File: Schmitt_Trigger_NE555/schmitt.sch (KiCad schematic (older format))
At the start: 8 parts, among them J1 CONN_01X02, J2 Vcc, U1 LM555N

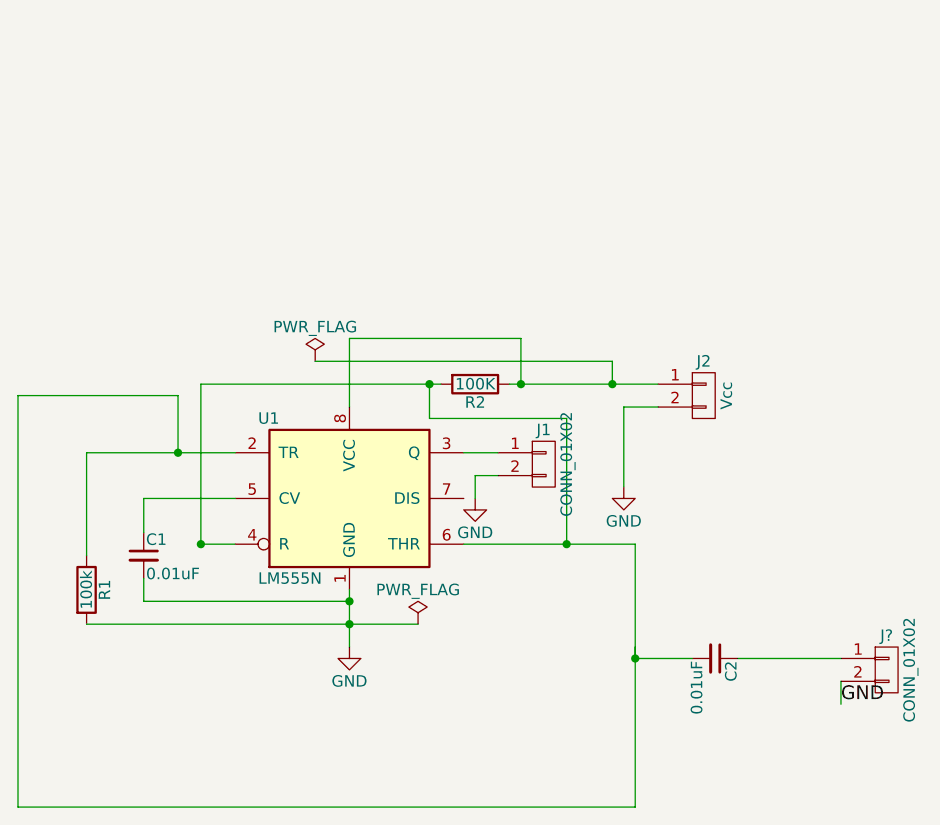
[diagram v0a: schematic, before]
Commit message: Added Schmitt Trigger Using NE555 PCB Layout
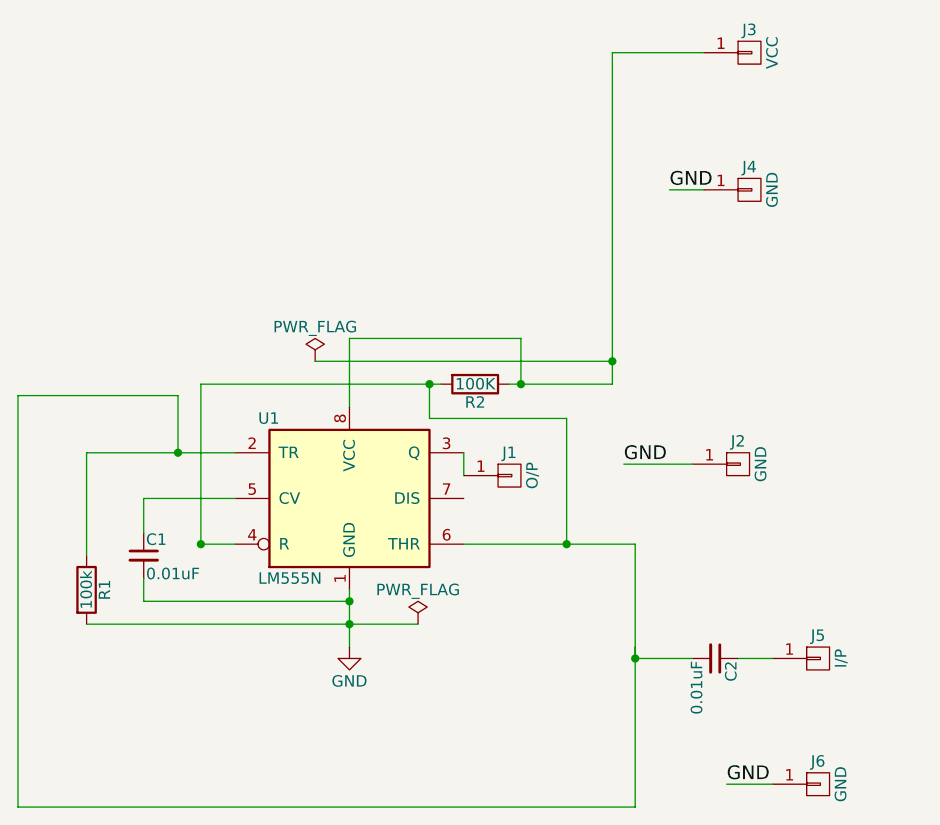
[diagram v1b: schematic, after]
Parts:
- removed J1: CONN_01X02, Connectors_Terminal_Blocks:TerminalBlock_Pheonix_MKDS1.5-2pol, symbol CONN_01X02
- removed J2: Vcc, Connectors_Terminal_Blocks:TerminalBlock_Pheonix_MKDS1.5-2pol, symbol CONN_01X02
- removed J?: CONN_01X02, symbol CONN_01X02
- added J1: O/P, Connectors:Banana_Jack_1Pin, symbol CONN_01X01
- added J2, J4, J6: GND, Connectors:Banana_Jack_1Pin, symbol CONN_01X01
- added J3: VCC, Connectors:Banana_Jack_1Pin, symbol CONN_01X01
- added J5: I/P, Connectors:Banana_Jack_1Pin, symbol CONN_01X01
- R1, R2: footprint (none) -> Resistors_THT:R_Axial_DIN0207_L6.3mm_D2.5mm_P15.24mm_Horizontal
- U1: footprint (none) -> Housings_DIP:DIP-8_W7.62mm
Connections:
- net GND: now also J2.1 (P1), J4.1 (P1), J6.1 (P1)
- net at U1.3 (Q): now also J1.1 (P1)
- net at R2.1, U1.8 (VCC): now also J3.1 (P1)
- net at C2.1: now also J5.1 (P1)
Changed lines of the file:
@@
 LIBS:contrib
 LIBS:valves
+LIBS:schmitt-cache
 EELAYER 25 0
 EELAYER END
@@
 F 0 "U1" H 6100 4800 50  0000 L CNN
 F 1 "LM555N" H 6100 4100 50  0000 L CNN
-F 2 "" H 6500 4450 50  0001 C CNN
+F 2 "Housings_DIP:DIP-8_W7.62mm" H 6500 4450 50  0001 C CNN
 F 3 "" H 6500 4450 50  0001 C CNN
 	1    6500 4450
@@
 F 0 "R1" V 5430 4850 50  0000 C CNN
 F 1 "100k" V 5350 4850 50  0000 C CNN
-F 2 "" V 5280 4850 50  0001 C CNN
+F 2 "Resistors_THT:R_Axial_DIN0207_L6.3mm_D2.5mm_P15.24mm_Horizontal" V 5280 4850 50  0001 C CNN
 F 3 "" H 5350 4850 50  0001 C CNN
 	1    5350 4850
@@
 F 0 "R2" V 7130 3950 50  0000 C CNN
 F 1 "100K" V 7050 3950 50  0000 C CNN
-F 2 "" V 6980 3950 50  0001 C CNN
+F 2 "Resistors_THT:R_Axial_DIN0207_L6.3mm_D2.5mm_P15.24mm_Horizontal" V 6980 3950 50  0001 C CNN
 F 3 "" H 7050 3950 50  0001 C CNN
 	1    7050 3950
@@
 $EndComp
 $Comp
-L CONN_01X02 J2
-U 1 1 59E313DE
-P 8050 4000
-F 0 "J2" H 8050 4150 50  0000 C CNN
-F 1 "Vcc" V 8150 4000 50  0000 C CNN
-F 2 "Connectors_Terminal_Blocks:TerminalBlock_Pheonix_MKDS1.5-2pol" H 8050 4000 50  0001 C CNN
-F 3 "" H 8050 4000 50  0001 C CNN
-	1    8050 4000
-	1    0    0    -1
-$EndComp
-$Comp
-L GND #PWR02
-U 1 1 59E314A2
-P 7700 4400
-F 0 "#PWR02" H 7700 4150 50  0001 C CNN
-F 1 "GND" H 7700 4250 50  0000 C CNN
-F 2 "" H 7700 4400 50  0001 C CNN
-F 3 "" H 7700 4400 50  0001 C CNN
-	1    7700 4400
-	1    0    0    -1
-$EndComp
-$Comp
-L CONN_01X02 J1
-U 1 1 59E31594
-P 7350 4300
-F 0 "J1" H 7350 4450 50  0000 C CNN
-F 1 "CONN_01X02" V 7450 4300 50  0000 C CNN
-F 2 "Connectors_Terminal_Blocks:TerminalBlock_Pheonix_MKDS1.5-2pol" H 7350 4300 50  0001 C CNN
-F 3 "" H 7350 4300 50  0001 C CNN
-	1    7350 4300
-	1    0    0    -1
-$EndComp
-$Comp
-L GND #PWR03
-U 1 1 59E31634
-P 7050 4450
-F 0 "#PWR03" H 7050 4200 50  0001 C CNN
-F 1 "GND" H 7050 4300 50  0000 C CNN
-F 2 "" H 7050 4450 50  0001 C CNN
-F 3 "" H 7050 4450 50  0001 C CNN
-	1    7050 4450
-	1    0    0    -1
-$EndComp
-$Comp
-L PWR_FLAG #FLG04
+L PWR_FLAG #FLG02
 U 1 1 59E31DB9
 P 6350 3850
-F 0 "#FLG04" H 6350 3925 50  0001 C CNN
+F 0 "#FLG02" H 6350 3925 50  0001 C CNN
 F 1 "PWR_FLAG" H 6350 4000 50  0000 C CNN
 F 2 "" H 6350 3850 50  0001 C CNN
@@
 $EndComp
 $Comp
-L PWR_FLAG #FLG05
+L PWR_FLAG #FLG03
 U 1 1 59E31FED
 P 6800 5000
-F 0 "#FLG05" H 6800 5075 50  0001 C CNN
+F 0 "#FLG03" H 6800 5075 50  0001 C CNN
 F 1 "PWR_FLAG" H 6800 5150 50  0000 C CNN
 F 2 "" H 6800 5000 50  0001 C CNN
@@
 Connection ~ 7750 5150
 Wire Wire Line
-	8200 5150 8650 5150
-Wire Wire Line
 	5850 4650 5850 3950
-Wire Wire Line
-	7200 3950 7850 3950
 Wire Wire Line
 	6850 3950 6850 4100
@@
 Connection ~ 6850 3950
 Wire Wire Line
-	7850 4050 7700 4050
-Wire Wire Line
-	7000 4250 7150 4250
-Wire Wire Line
-	7150 4350 7050 4350
-Wire Wire Line
-	7050 4350 7050 4450
-Wire Wire Line
-	7700 4050 7700 4400
-Wire Wire Line
 	6350 3850 7650 3850
 Wire Wire Line
-	7650 3850 7650 3950
-Connection ~ 7650 3950
-Wire Wire Line
 	5850 3950 6900 3950
 Wire Wire Line
@@
 Wire Wire Line
 	7250 3750 7250 3950
+$Comp
+L CONN_01X01 J3
+U 1 1 59E34C66
+P 8250 2500
+F 0 "J3" H 8250 2600 50  0000 C CNN
+F 1 "VCC" V 8350 2500 50  0000 C CNN
+F 2 "Connectors:Banana_Jack_1Pin" H 8250 2500 50  0001 C CNN
+F 3 "" H 8250 2500 50  0001 C CNN
+	1    8250 2500
+	1    0    0    -1
+$EndComp
+$Comp
+L CONN_01X01 J4
+U 1 1 59E34D8F
+P 8250 3100
+F 0 "J4" H 8250 3200 50  0000 C CNN
+F 1 "GND" V 8350 3100 50  0000 C CNN
+F 2 "Connectors:Banana_Jack_1Pin" H 8250 3100 50  0001 C CNN
+F 3 "" H 8250 3100 50  0001 C CNN
+	1    8250 3100
+	1    0    0    -1
+$EndComp
+$Comp
+L CONN_01X01 J1
+U 1 1 59E34EB7
+P 7200 4350
+F 0 "J1" H 7200 4450 50  0000 C CNN
+F 1 "O/P" V 7300 4350 50  0000 C CNN
+F 2 "Connectors:Banana_Jack_1Pin" H 7200 4350 50  0001 C CNN
+F 3 "" H 7200 4350 50  0001 C CNN
+	1    7200 4350
+	1    0    0    -1
+$EndComp
+$Comp
+L CONN_01X01 J2
+U 1 1 59E34F50
+P 8200 4300
+F 0 "J2" H 8200 4400 50  0000 C CNN
+F 1 "GND" V 8300 4300 50  0000 C CNN
+F 2 "Connectors:Banana_Jack_1Pin" H 8200 4300 50  0001 C CNN
+F 3 "" H 8200 4300 50  0001 C CNN
+	1    8200 4300
+	1    0    0    -1
+$EndComp
+$Comp
+L CONN_01X01 J5
+U 1 1 59E34FCB
+P 8550 5150
+F 0 "J5" H 8550 5250 50  0000 C CNN
+F 1 "I/P" V 8650 5150 50  0000 C CNN
+F 2 "Connectors:Banana_Jack_1Pin" H 8550 5150 50  0001 C CNN
+F 3 "" H 8550 5150 50  0001 C CNN
+	1    8550 5150
+	1    0    0    -1
+$EndComp
+$Comp
+L CONN_01X01 J6
+U 1 1 59E34FFA
+P 8550 5700
+F 0 "J6" H 8550 5800 50  0000 C CNN
+F 1 "GND" V 8650 5700 50  0000 C CNN
+F 2 "Connectors:Banana_Jack_1Pin" H 8550 5700 50  0001 C CNN
+F 3 "" H 8550 5700 50  0001 C CNN
+	1    8550 5700
+	1    0    0    -1
+$EndComp
+Wire Wire Line
+	8050 2500 7650 2500
+Wire Wire Line
+	7650 2500 7650 3950
+Wire Wire Line
+	7650 3950 7200 3950
+Connection ~ 7650 3850
 Connection ~ 7250 3950
-$Comp
-L CONN_01X02 J?
-U 1 1 59E33474
-P 8850 5200
-F 0 "J?" H 8850 5350 50  0000 C CNN
-F 1 "CONN_01X02" V 8950 5200 50  0000 C CNN
-F 2 "" H 8850 5200 50  0001 C CNN
-F 3 "" H 8850 5200 50  0001 C CNN
-	1    8850 5200
-	1    0    0    -1
-$EndComp
-Wire Wire Line
-	8650 5250 8650 5350
-Text Label 8650 5350 0    60   ~ 0
+Wire Wire Line
+	8050 3100 7900 3100
+Text Label 7900 3100 0    60   ~ 0
+GND
+Wire Wire Line
+	7000 4250 7000 4350
+Wire Wire Line
+	8000 4300 7700 4300
+Text Label 7700 4300 0    60   ~ 0
+GND
+Wire Wire Line
+	8350 5150 8200 5150
+Wire Wire Line
+	8350 5700 8150 5700
+Text Label 8150 5700 0    60   ~ 0
 GND
 $EndSCHEMATC
